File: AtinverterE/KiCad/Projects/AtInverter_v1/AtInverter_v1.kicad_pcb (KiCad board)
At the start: 2 copper layers, 83.8 x 94.6 mm, 60 parts

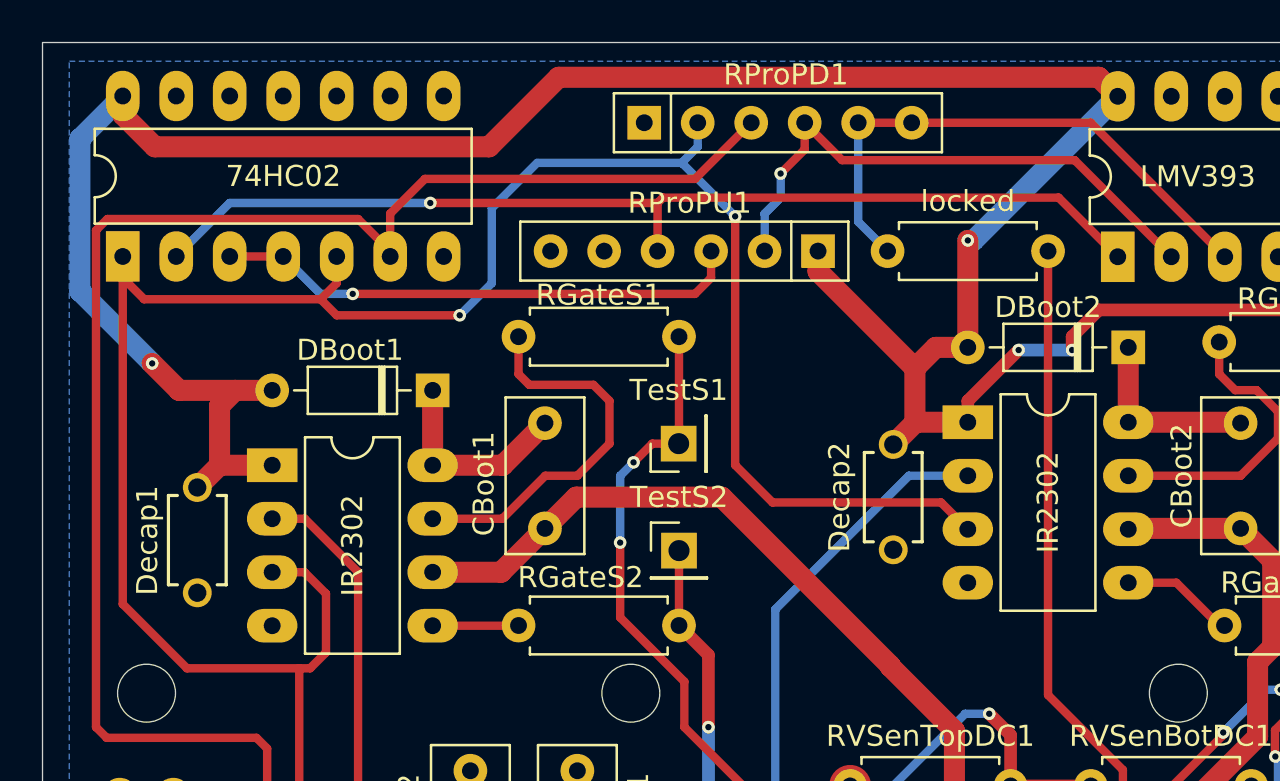
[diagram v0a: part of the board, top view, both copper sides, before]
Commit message: Changed footprint for IR2302 to SMD
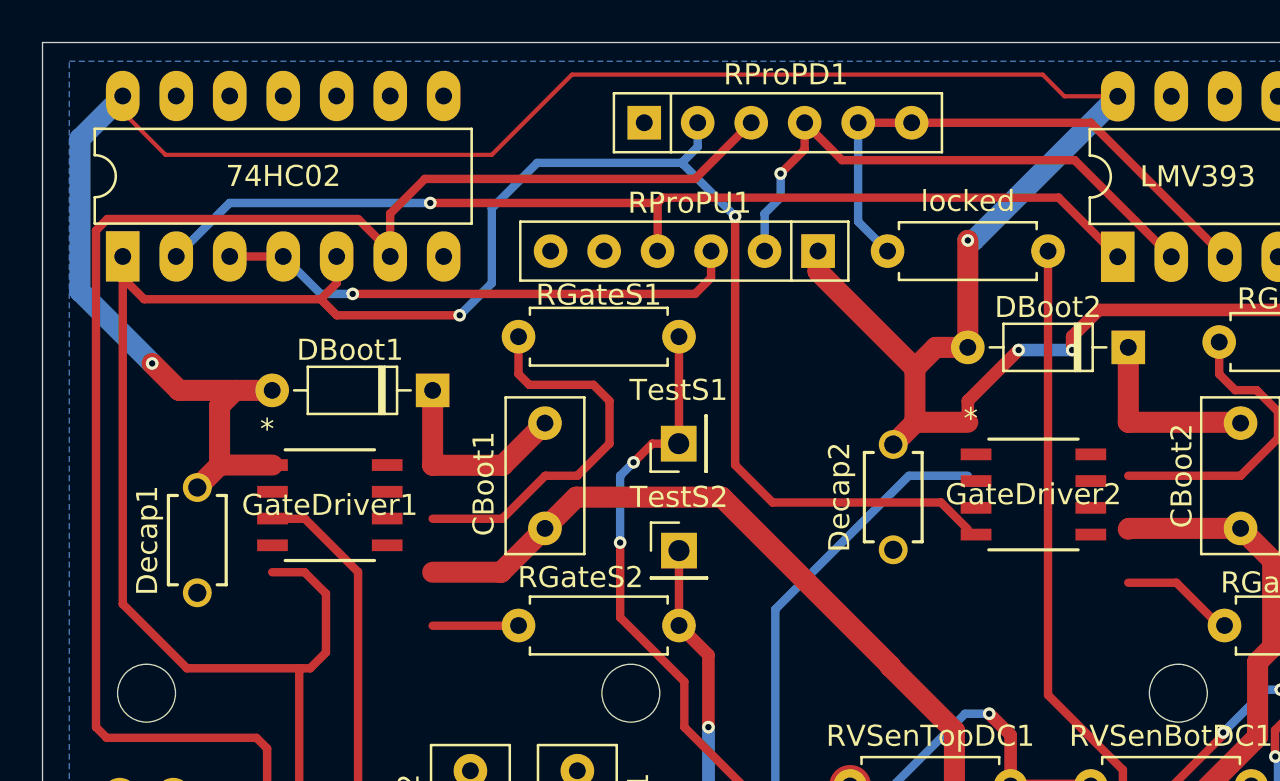
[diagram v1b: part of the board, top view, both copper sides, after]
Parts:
- GateDriver1, GateDriver2: footprint Package_DIP:DIP-8_W7.62mm_LongPads -> Atinverter_vE:PG-DSO-8-910_INF
- moved GateDriver2 4.63 mm to (110.6, 63.4)
- moved GateDriver1 3.33 mm to (77.1, 63.9)
